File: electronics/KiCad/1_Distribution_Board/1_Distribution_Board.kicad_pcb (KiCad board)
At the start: 2 copper layers, 130 x 120 mm, 189 parts, among them CN1 HC-5264-3A, CN2 HC-5264-3A, J1 JST VH, J10 Generic 2.54mm, J11 Generic 2.54mm, J12 Conn_01x06, J13 Conn_01x10, J14 2.54-1*4P母, J15 2.54-1*4P母, J16 PM254V-11-06-H85, J17 Conn_02x08_Odd_Even, J18 PM254V-11-06-H85, J19 2.54-1*4P母, J2 JST VH, J20 2.54-1*4P母, J21 Jumper Pins, J22 Jumper Pins, J23 JST PH, J24 Generic 2.54mm, J25 Jumper Pins, J26 Jumper Pins, J27 JST PH, J28 Generic 2.54mm, J29 Jumper Pins, J3 JST VH, J30 Jumper Pins, J31 JST PH, J32 Generic 2.54mm, J33 Jumper Pins, J34 Jumper Pins, J35 JST PH, J36 Generic 2.54mm, J37 Jumper Pins, J38 Jumper Pins, J39 JST PH, J4 Conn_01x04, J40 Generic 2.54mm, J5 Generic 2.54mm, J6 Generic 2.54mm, J8 Generic 2.54mm, J9 Generic 2.54mm, M1 MountingHole_3.2mm_M3_ISO7380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, P1 Header-Female-2.54_1x8, P10 Header-Female-2.54_1x8, P11 Header-Female-2.54_1x2, P12 Header-Female-2.54_1x8, P13 Header-Female-2.54_1x8, P14 Header-Female-2.54_1x2, P15 Header-Female-2.54_1x8, P2 Header-Female-2.54_1x2, P3 Header-Female-2.54_1x8, P4 Header-Female-2.54_1x8, P5 Header-Female-2.54_1x2, P6 Header-Female-2.54_1x8, P7 Header-Female-2.54_1x8, P8 Header-Female-2.54_1x2, P9 Header-Female-2.54_1x8, Q1 DMG2305UX, Q2 AO3400A, Q3 AO3400A, Q4 AO3400A, Q5 AO3400A, U1 KH-2.54FH-1X20P-H8.5, U2 KH-2.54FH-1X20P-H8.5, U3 R-78C5.0-1.0, U4 R-78B12-2.0, U5 R-78B6.5-1.5, U6 PCA9306, U7 PCA9685PW, Y1 25MHz

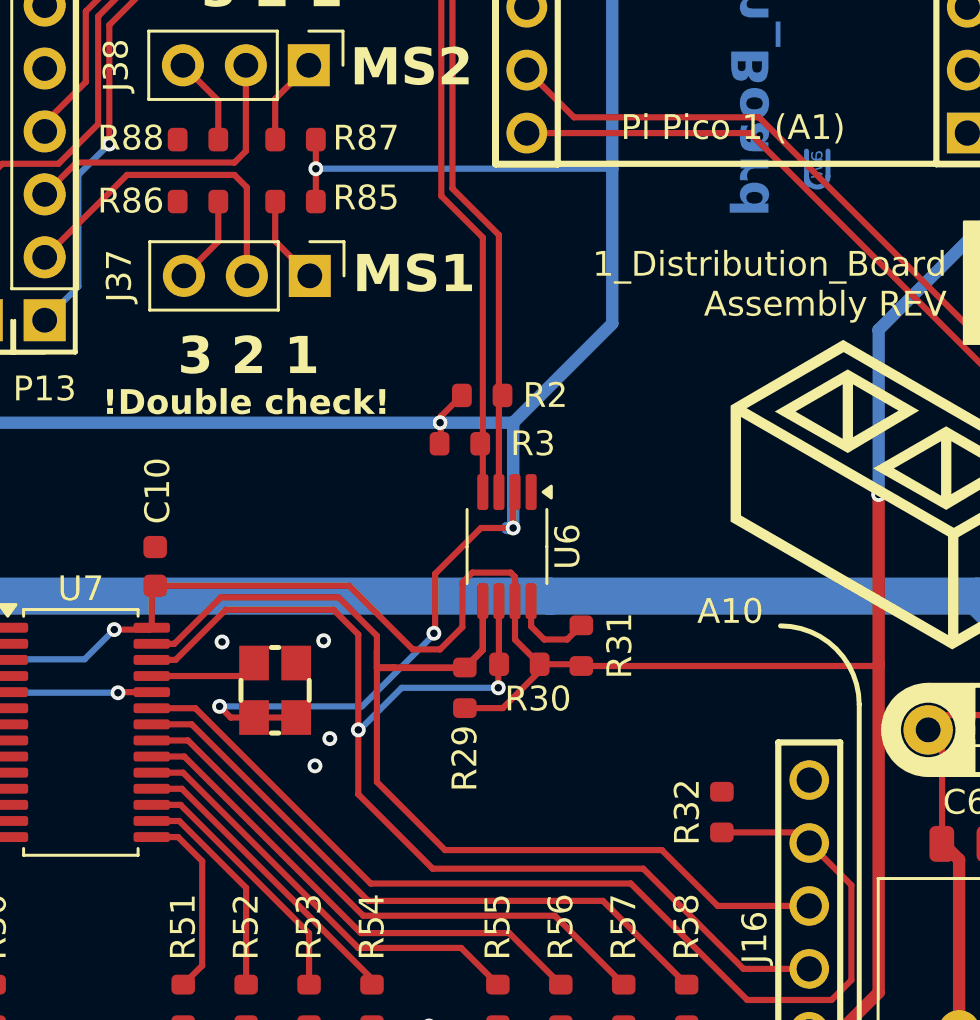
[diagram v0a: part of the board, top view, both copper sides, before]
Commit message: Updated to reflect V1.0 of layer board as well
Updated for initial orders with PCA module populated. Also updated to layer boards for flex cables.
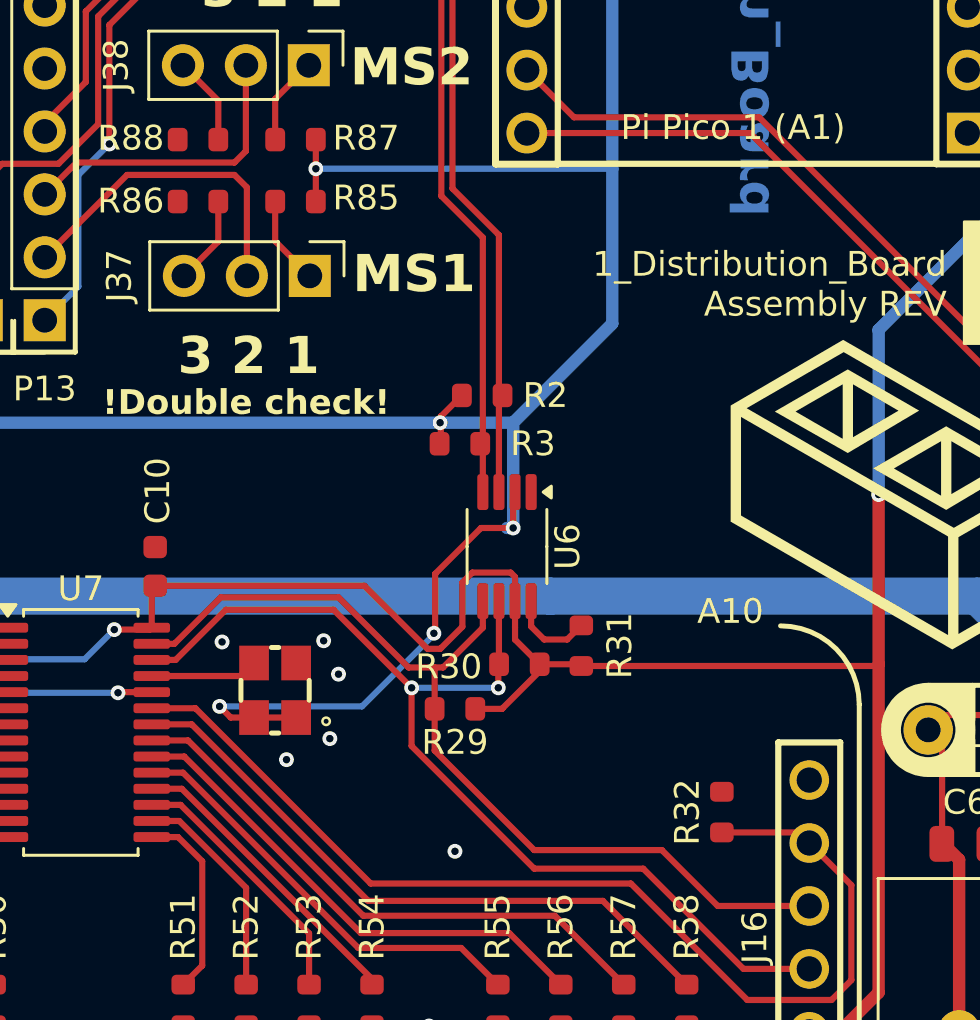
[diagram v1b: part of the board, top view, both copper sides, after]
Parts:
- removed JAW: Maker's Mark, JAW:JAW
- moved R29 0.94 mm to (72.9, 99.0), turned to 180 degrees
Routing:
- net /PCA9685 Module/I2C0_SDA_5V: track 50.5 -> 38.2 mm
- net /PCA9685 Module/I2C0_SCL_5V: track 47.4 -> 42.1 mm
- net GND: vias 55 -> 57

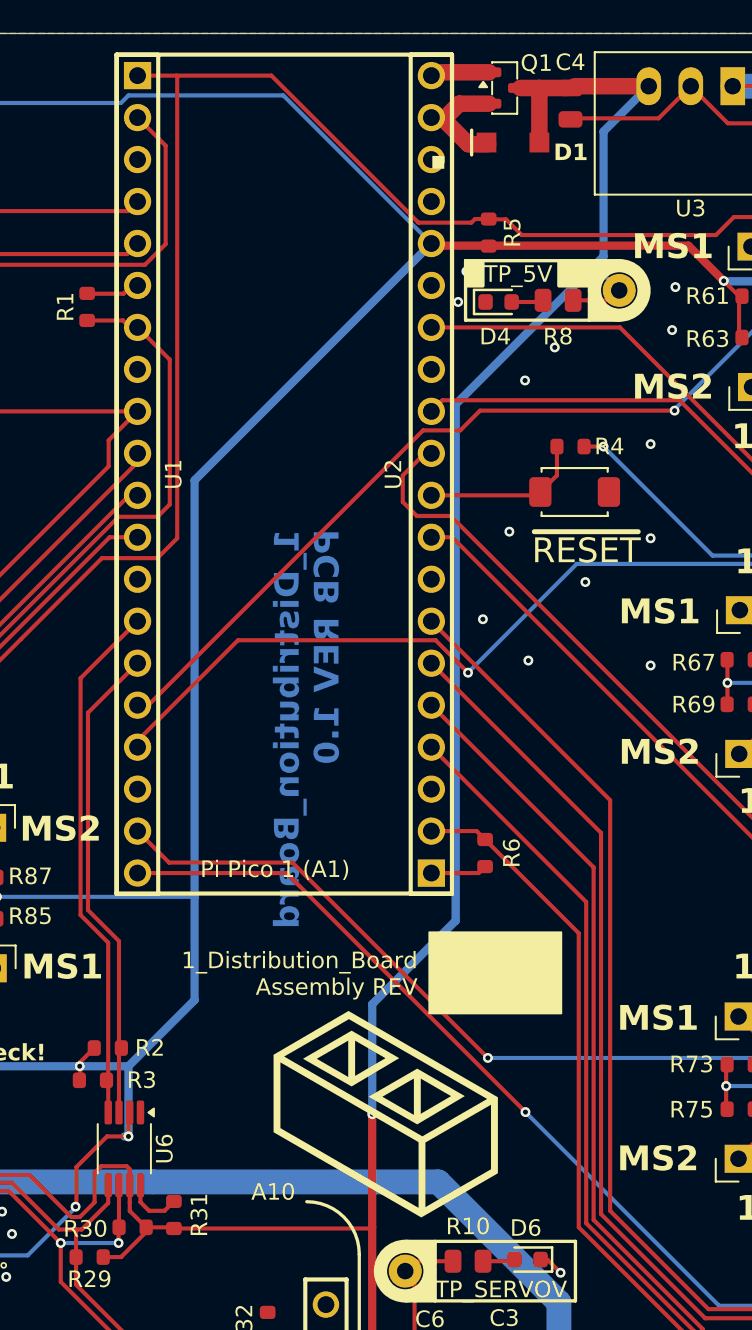
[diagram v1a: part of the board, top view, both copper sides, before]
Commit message: Corrected SCH for power sequence issue
5V to Vsys for all powered items.
Correction of the PCA9306 power pins.
Added decoupling to oscillator and PCA9306.
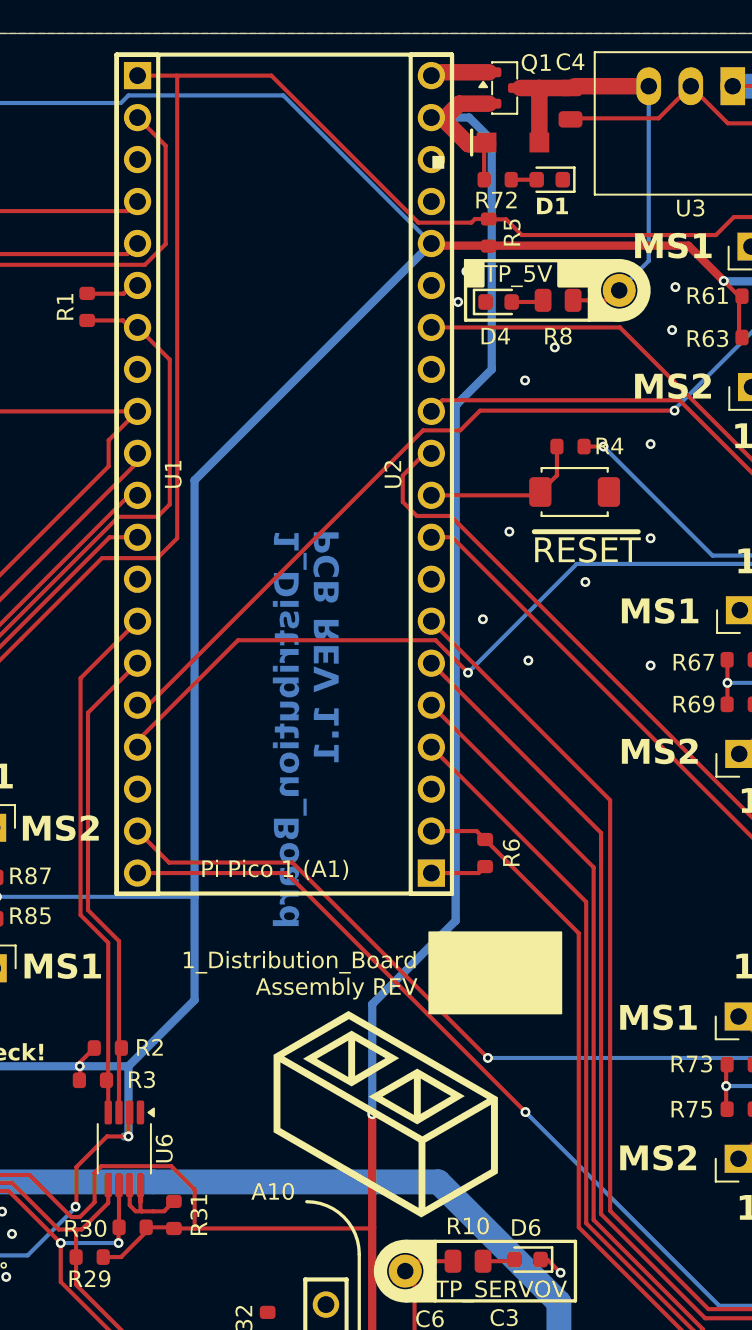
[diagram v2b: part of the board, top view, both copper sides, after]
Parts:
- added D7: Yellow, PCM_JLCPCB:D_0603, F.Cu at (100.7, 33.8)
- added R72: 300Ω, PCM_JLCPCB:R_0603, F.Cu at (97.6, 33.8)
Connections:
- C10 pad 1: +5V -> VSYS
- D1 pad 1: /VSYS -> VSYS
- J16 pad 2: +5V -> VSYS
- Q1 pad 2: /VSYS -> VSYS
- R29 pad 1: +5V -> VSYS
- R30 pad 1: +5V -> VSYS
- R31 pad 1: +5V -> VSYS
- R33 pad 1: +5V -> VSYS
- R35 pad 1: +5V -> VSYS
- R37 pad 1: +5V -> VSYS
- R39 pad 1: +5V -> VSYS
- R41 pad 1: +5V -> VSYS
- R59 pad 1: +5V -> VSYS
- U2 pad 19: /VSYS -> VSYS
- U6 pad 7: +5V -> Net-(U6-EN)
- U7 pad 28: +5V -> VSYS
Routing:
- net VSYS: track 0.00 -> 169.8 mm, vias 0 -> 3
- net +5V: track 177.5 -> 27.4 mm, vias 3 -> 0
- net /VSYS: track 6.48 -> 0.00 mm
- net Net-(U6-EN): track 3.50 -> 6.87 mm
- net Net-(D7-Pad2): track 0.00 -> 1.54 mm
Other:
- board text added: "1_Distribution_Board PCB REV 1.1"
- board text removed: "1_Distribution_Board PCB REV 1.0"

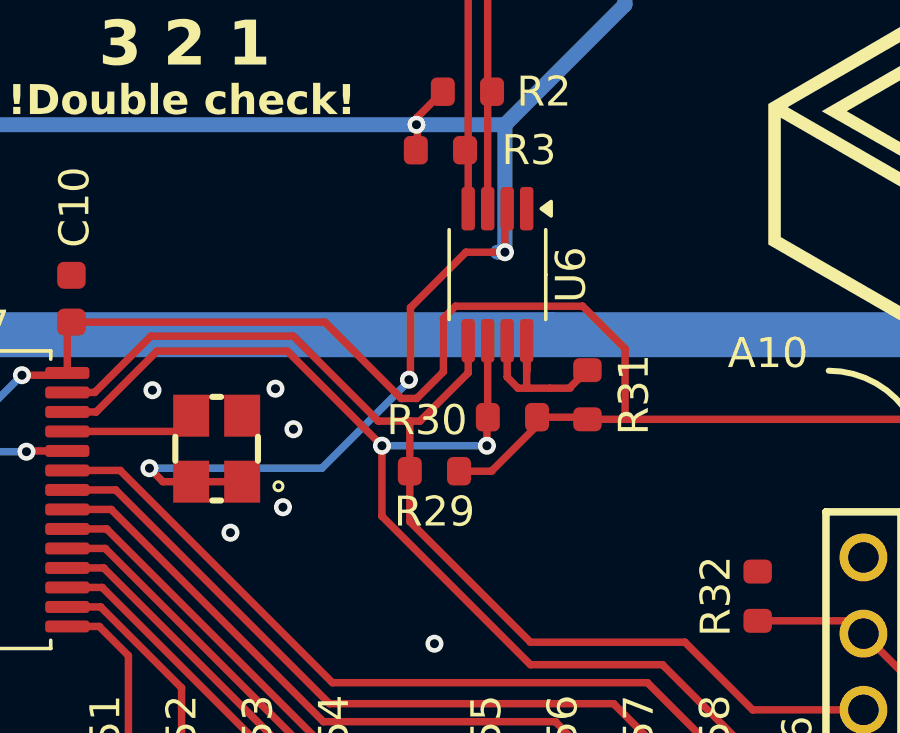
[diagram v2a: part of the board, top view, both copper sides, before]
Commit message: Updated for changes to the SCH items
Updated PCB to include all changed from the SCH.
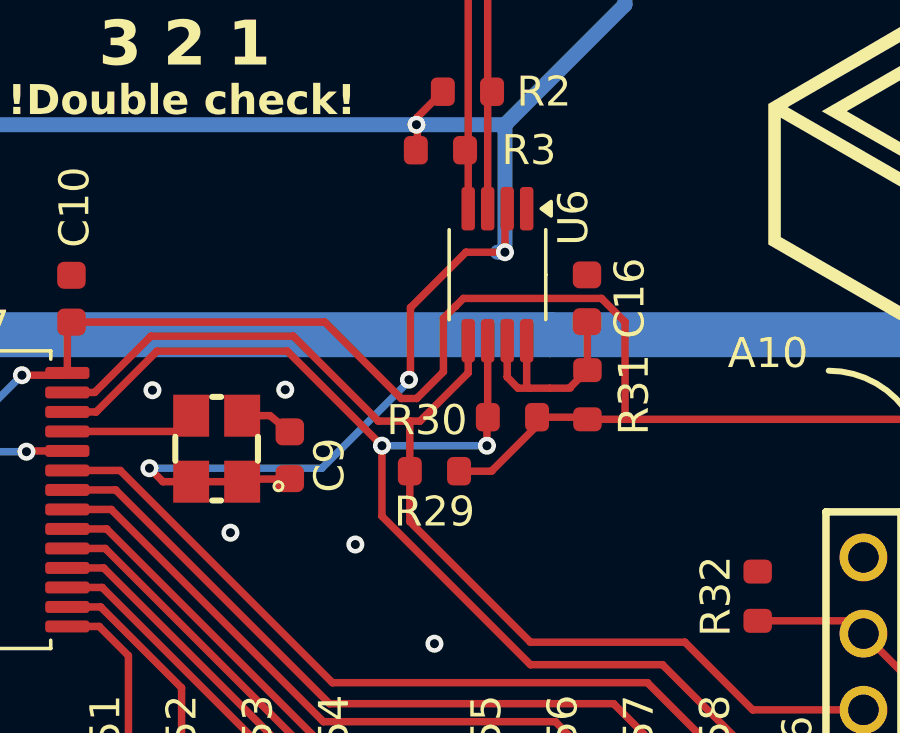
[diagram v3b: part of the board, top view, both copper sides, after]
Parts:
- added C16: 100nF, PCM_JLCPCB:C_0603, F.Cu at (78.0, 93.3)
- added C9: 100nF, PCM_JLCPCB:C_0603, F.Cu at (68.1, 98.5)
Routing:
- net GND: track 107.2 -> 109.3 mm, vias 57 -> 56
- net +3V3: track 476.5 -> 478.5 mm
- net VSYS: track 169.8 -> 170.5 mm
- net Net-(U6-EN): track 6.87 -> 7.47 mm
